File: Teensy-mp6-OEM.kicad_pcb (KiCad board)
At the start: 2 copper layers, 64.8 x 24.8 mm, 4 parts, among them J1 CONN_01X03, U1 Teensy_3.2, U2 mp6-OEM, U3 mp6-pump-conector

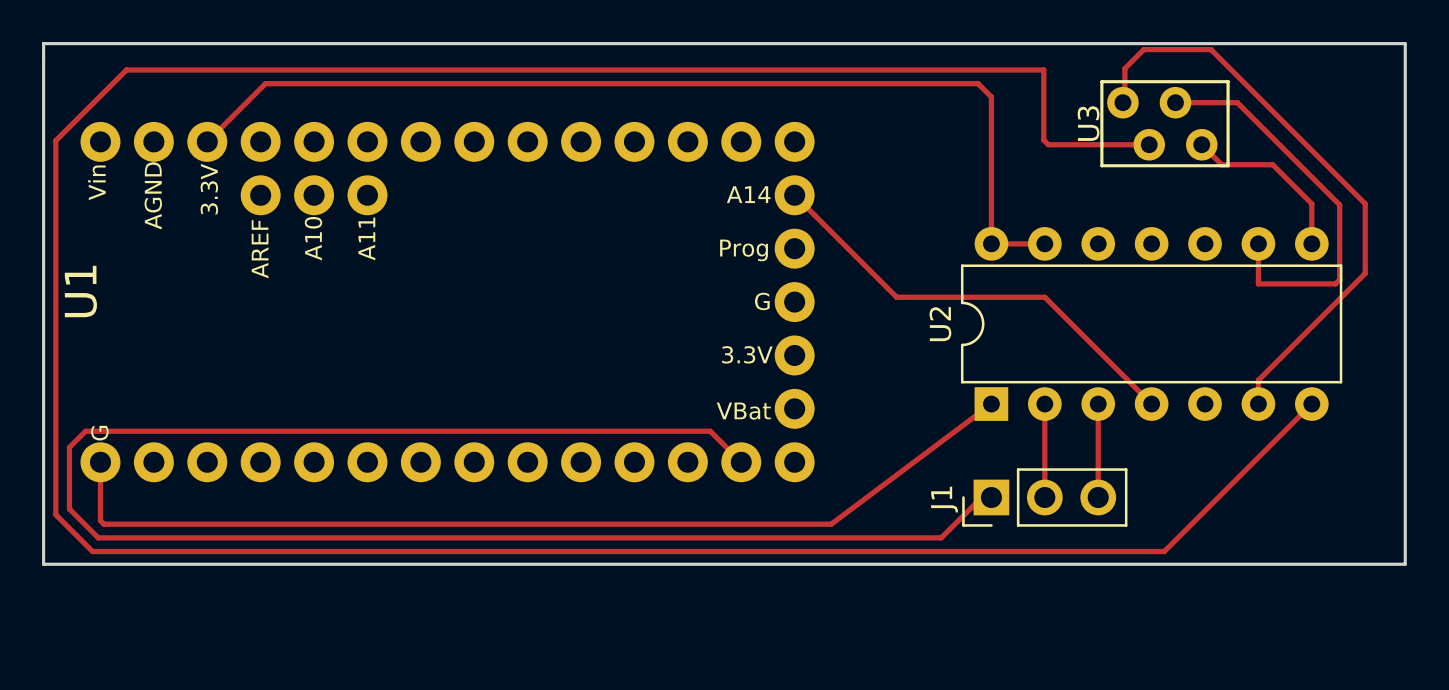
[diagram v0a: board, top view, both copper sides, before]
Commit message: Swap top and bottom layers and flip board
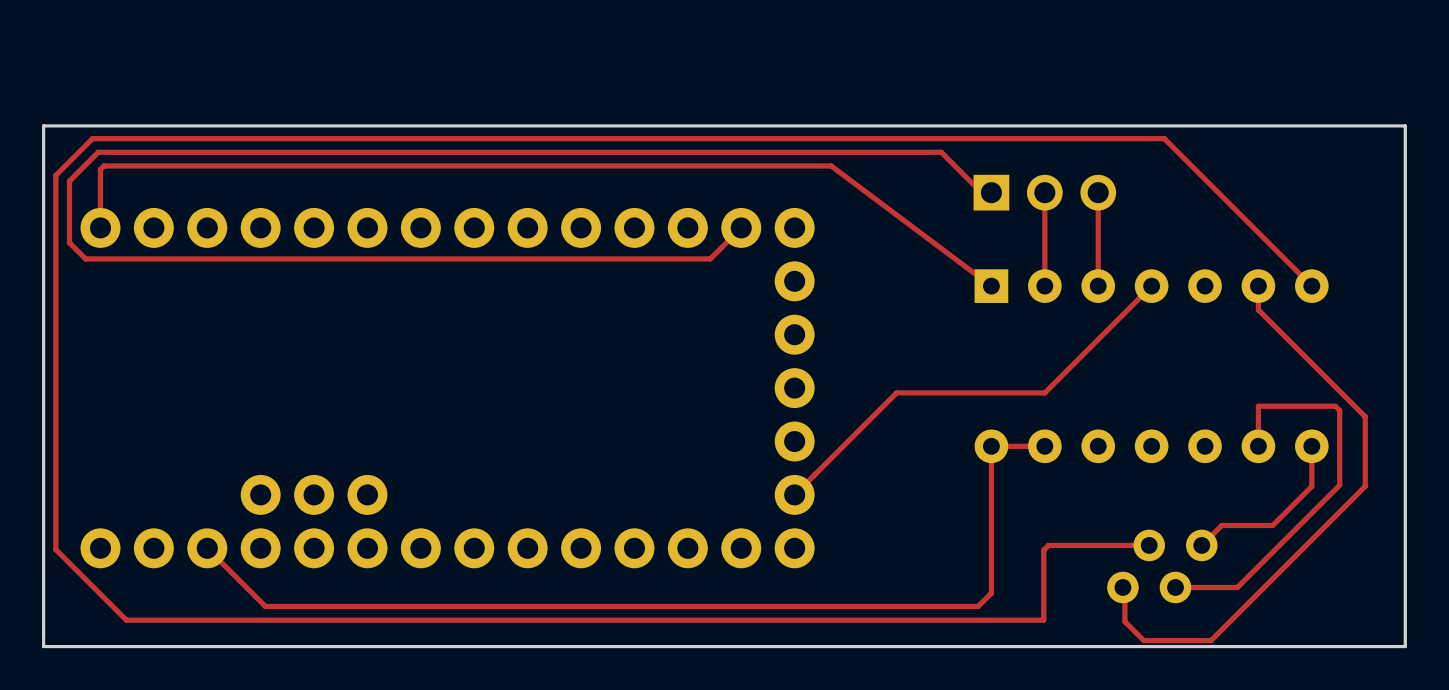
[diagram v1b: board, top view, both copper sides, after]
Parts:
- J1, U1, U2, U3: moved to B.Cu
- moved U3 21.1 mm to (182.9, 117.6), turned to 270 degrees
- moved J1 14.5 mm to (174.6, 99.8), turned to 270 degrees
- moved U2 5.61 mm to (174.6, 104.2), turned to 270 degrees
- moved U1 4.09 mm to (148.5, 109.1)
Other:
- outline, holes or cut-outs redrawn
